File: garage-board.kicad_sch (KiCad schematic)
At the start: 17 parts, among them J1 Input, M1 Motor_DC, U1 Pololu_H2_36v11_CS, U2 ESP32-C6-DEV-KIT-N8, U3 Pololu-5266

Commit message: kicad: claude clean up
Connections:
- net GND: now also HS1.3 (GND), U2.32 (GND), U3.2 (GND); no longer HS1. (GND), U3. (EN)
- net +31V: now reaches C2.1, D1.4 (+), D2.1 (A1), R3.2, U1.9 (VIN)
- net +31V: now also U3.3 (VIN); no longer U3. (EN)
- net at R1.2, R2.1: now also HS1.1 (A); no longer HS1. (GND)
- net PWMB: now reaches U1.2 (PWMB), U2.26 (IO21)
- net PWMA: now reaches U1.3 (PWMA), U2.25 (IO20)
- net ~{SLP}: now reaches U1.4 (~{SLP}), U2.24 (IO19)
- net ~{FLT}: now reaches U1.5 (~{FLT}), U2.23 (IO18)
- net CS: now reaches U1.6 (CS), U2.12 (IO2)
- net 3V3 renamed +3V3
- net +3V3: now also HS1.2 (+), U3.1 (VOUT); no longer HS1. (GND), U3. (EN)
- no-connect marks 0 -> 22
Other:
- note added: "24 V AC"
- note added: "24 V AC INPUT & RECTIFIER"
- note added: "3.3 V REGULATOR"
- note added: "ESP32-C6 MCU"
- note added: "HALL SENSOR"
- note added: "MOTOR DRIVER"
- title: (none) -> Garage board
- moved on the sheet: C1, C2, C3, C4, D1, D2, F1, J1, M1, R1, R2, R3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

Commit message: Change to 5V and power issues
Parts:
- removed M1: Motor_DC, symbol Motor:Motor_DC
- added C5: 470uF 105C ESR, symbol Device:C_Polarized
- added C6: 100nF, symbol Device:C
- added D3: 1N4007, Diode_THT:D_DO-41_SOD81_P10.16mm_Horizontal, symbol Diode:1N4007
- added J2: Motor, symbol Connector_Generic:Conn_01x03
- added J5: btn0, symbol Connector_Generic:Conn_01x02
- added R5: 4.7k, symbol Device:R
- added R6: 1k, symbol Device:R
- C1: value 470uF -> 470uF 105C ESR
- C2: value 470uF -> 4700uF 105C ESR
- C3: value 2.2nF -> 100nF
- HS1: value (none) -> HAL503
- J1: value Input -> 24VAC
- R2: value 1k -> 10k
- R3: value 10k -> 10k (0.5W)
- R4: value 10k -> 4.7k
- U3: value Pololu-5266 -> Pololu-5267; symbol garage_board_symbols:Pololu-5266 -> garage_board_symbols:Pololu-5267
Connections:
- net +31V: now also D3.2 (A); no longer U3.3 (VIN)
- net +3V3: now also R5.1; no longer C4.2, HS1.2 (+), U3.1 (VOUT)
- net GND: now also C5.2, C6.2, J2.3 (Pin_3), J5.1 (Pin_1); no longer C1.2
- net at U1.10 (OUTA): now also J2.2 (Pin_2)
- net at U1.11 (OUTB): now also J2.1 (Pin_1)
- net +5V: now reaches U2.14 (5V)
- net +5V: now also C4.2, HS1.2 (+), U3.1 (VOUT)
- net at U2.5 (IO6): now also C6.1, R5.2, R6.2
- net CS: no longer names the net of U1.6 (CS), U2.12 (IO2)
- net PWMA: no longer names the net of U1.3 (PWMA), U2.25 (IO20)
- net PWMB: no longer names the net of U1.2 (PWMB), U2.26 (IO21)
- net ~{FLT}: no longer names the net of U1.5 (~{FLT}), U2.23 (IO18)
- net ~{SLP}: no longer names the net of U1.4 (~{SLP}), U2.24 (IO19)
- net ~{SLP}: now also R4.1
- new net: J5.2 (Pin_2), R6.1
- new net: C5.1, D3.1 (K), U3.3 (VIN)
- new net: C1.2, U1.13 (-)
- new net: C1.1, U1.14 (+)
- now unconnected: U1.8 (VM)
- no-connect marks 22 -> 21
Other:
- note added: "LOGIC SUPPLY 5 V"
- note removed: "24 V AC"
- note removed: "3.3 V REGULATOR"
- moved on the sheet: C1, D2, R3, U3

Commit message: Add LAMP
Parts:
- added D4: 1N4148, Diode_THT:D_DO-35_SOD27_P7.62mm_Horizontal, symbol Diode:1N4148
- added K1: G5Q-1A, Relay_THT:Relay_SPST_Omron-G5Q-1A, symbol Relay:G5Q-1A
- added LA1: Lamp, symbol Device:Lamp
- added Q1: BC547, Package_TO_SOT_THT:TO-92_Inline, symbol Transistor_BJT:BC547
- added R7: 4.7k, symbol Device:R
- added R8: 680, symbol Device:R
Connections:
- net GND: now also Q1.3 (E)
- net at J1.1 (Pin_1): now also F1.2; no longer D1.3
- net at J1.2 (Pin_2): now also D1.2, K1.3; no longer F1.1
- net at C3.1, R2.2: now also U2.11 (IO11); no longer U2.10 (IO10)
- net at C6.1, R5.2, R6.2: now also U2.10 (IO10); no longer U2.5 (IO6)
- net at C5.1, D3.1 (K), U3.3 (VIN): now also R8.2
- net at U2.6 (IO7): now also R7.2
- net +31V: no longer names the net of C2.1, D1.4 (+), D2.1 (A1), D3.2 (A), R3.2, U1.9 (VIN)
- new net: D4.2 (A), K1.5, Q1.1 (C)
- new net: Q1.2 (B), R7.1
- new net: D1.3, F1.1, LA1.2 (+)
- new net: D4.1 (K), K1.1, R8.1
- new net: K1.2, LA1.1 (-)
- no-connect marks 21 -> 20
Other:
- note added: "24 V AC"
- note added: "LAMP"
- note added: "UHE (or two 2200uF)"
- moved on the sheet: C1, C3, C4, C5, C6, D2, D3, HS1, J2, J5, R1, R2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

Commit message: Fix LED and sW
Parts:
- removed C6: 100nF, symbol Device:C
- removed J5: btn0, symbol Connector_Generic:Conn_01x02
- removed R6: 1k, symbol Device:R
- added D5: Red, symbol Device:LED
- added SW1, SW2, SW3: SW_Push, symbol Switch:SW_Push
- F1: value T8A -> T6.3A
- R5: value 4.7k -> 1k
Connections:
- net +3V3: no longer R5.1
- net GND: now also D5.1 (K), SW2.2, SW3.2
- net at R5.2: now also D5.2 (A); no longer U2.10 (IO10)
- net at U2.27 (IO22): now also SW2.1
- net at U2.28 (IO23): now also SW3.1
- new net: R5.1, U2.10 (IO10)
- no-connect marks 20 -> 18
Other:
- moved on the sheet: C5, D4, F1, K1, LA1, Q1, R4, R7, R8

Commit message: fix layout
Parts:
- removed SW1: SW_Push, symbol Switch:SW_Push
- C1, C5: value 470uF 105C ESR -> 470uF 63V 105C ESR
- C2: value 4700uF 105C ESR -> 4700uF 63V 105C ESR
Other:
- moved on the sheet: C5, D2, D4, D5, K1, LA1, Q1, R1, R3, R4, R5, R7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

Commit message: Add standard footprints
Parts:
- C1, C5: footprint (none) -> Capacitor_THT:CP_Radial_D12.5mm_P5.00mm
- C2: footprint (none) -> garage_board:CP_Radial_D25.0mm_P12.50mm
- C3, C4: footprint (none) -> Capacitor_THT:C_Disc_D5.0mm_W2.5mm_P5.00mm
- HS1: footprint (none) -> Connector_PinHeader_2.54mm:PinHeader_1x03_P2.54mm_Vertical
- J1: footprint (none) -> Connector_Molex:Molex_KK-396_A-41791-0003_1x03_P3.96mm_Vertical; symbol Connector_Generic:Conn_01x02 -> Connector_Generic:Conn_01x03
- J2: footprint (none) -> Connector_Molex:Molex_KK-396_A-41791-0003_1x03_P3.96mm_Vertical
- R1, R2, R4, R5, R7, R8: footprint (none) -> Resistor_THT:R_Axial_DIN0207_L6.3mm_D2.5mm_P10.16mm_Horizontal
- R3: footprint (none) -> Resistor_THT:R_Axial_DIN0414_L11.9mm_D4.5mm_P15.24mm_Horizontal
- U1: value Pololu_H2_36v11_CS -> Pololu-2993
- U2: footprint (none) -> PCM_Espressif:ESP32-C6-DevKitC-1; symbol garage_board_symbols:ESP32-C6-DEV-KIT-N8 -> PCM_Espressif:ESP32-C6-DevKitC-1
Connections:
- net at D1.2, K1.3: now also J1.3 (Pin_3); no longer J1.2 (Pin_2)
- no-connect marks 18 -> 19
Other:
- moved on the sheet: D5, R4, R5, SW2, SW3, U2

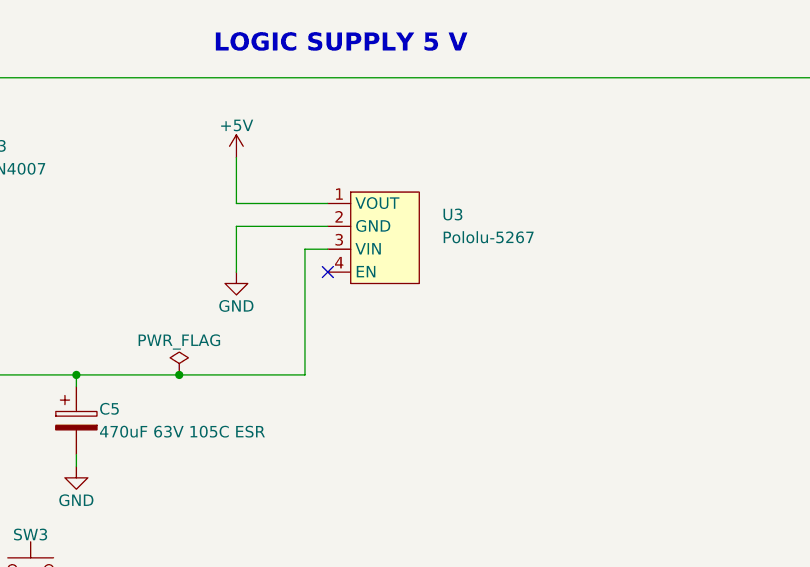
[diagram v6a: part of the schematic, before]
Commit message: Place components sketch on PCB
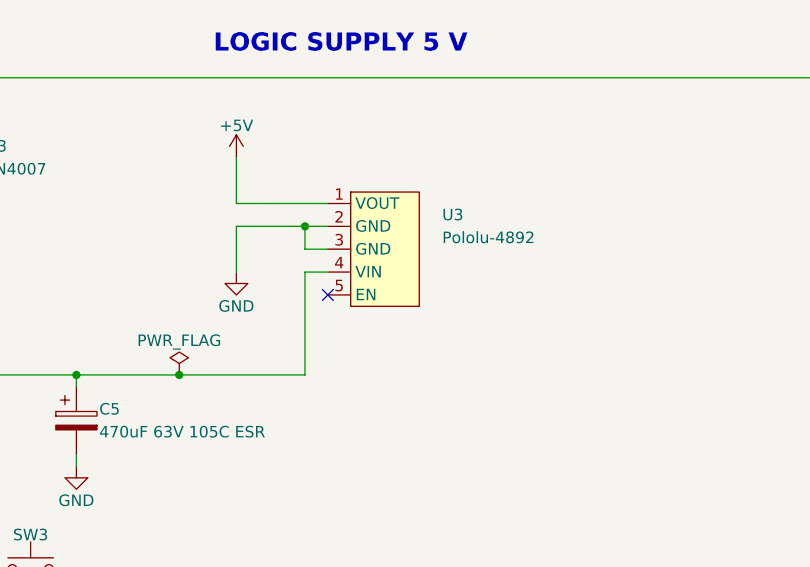
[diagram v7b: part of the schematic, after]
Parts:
- D5: footprint (none) -> garage_board:LED_D5.0mm_Horizontal
- F1: footprint (none) -> garage_board:Fuseholder_5x20mm_Lateral_P20.00x5.00mm
- LA1: footprint (none) -> garage_board:lamp
- SW2, SW3: footprint (none) -> garage_board:Switch
- U1: footprint (none) -> garage_board:Pololu Motor Driver 2993
- U3: value Pololu-5267 -> Pololu-4892; footprint (none) -> garage_board:Pololu 4892
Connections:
- net GND: now also U3.3 (GND)
- net at C5.1, D3.1 (K), R8.2: now also U3.4 (VIN); no longer U3.3 (VIN)
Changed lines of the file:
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@@
 	)
 	(junction
+		(at 210.82 49.53)
+		(diameter 0)
+		(color 0 0 0 0)
+	)
+	(junction
 		(at 27.94 45.72)
 		(diameter 0)
@@
 	)
 	(no_connect
-		(at 213.36 54.61)
+		(at 213.36 57.15)
 	)
 	(no_connect
@@
 	(wire
 		(pts
+			(xy 210.82 66.04) (xy 210.82 54.61)
+		)
+		(stroke
+			(width 0)
+			(type default)
+		)
+	)
+	(wire
+		(pts
 			(xy 165.1 120.65) (xy 170.18 120.65)
 		)
@@
 	(wire
 		(pts
+			(xy 210.82 49.53) (xy 203.2 49.53)
+		)
+		(stroke
+			(width 0)
+			(type default)
+		)
+	)
+	(wire
+		(pts
 			(xy 165.1 92.71) (xy 171.45 92.71)
 		)
@@
 	(wire
 		(pts
-			(xy 213.36 49.53) (xy 203.2 49.53)
+			(xy 213.36 49.53) (xy 210.82 49.53)
 		)
 		(stroke
@@
 	(wire
 		(pts
+			(xy 210.82 49.53) (xy 210.82 52.07)
+		)
+		(stroke
+			(width 0)
+			(type default)
+		)
+	)
+	(wire
+		(pts
 			(xy 185.42 135.89) (xy 185.42 119.38)
 		)
@@
 	(wire
 		(pts
+			(xy 210.82 54.61) (xy 213.36 54.61)
+		)
+		(stroke
+			(width 0)
+			(type default)
+		)
+	)
+	(wire
+		(pts
 			(xy 114.3 125.73) (xy 109.22 125.73)
 		)
@@
 	(wire
 		(pts
-			(xy 210.82 66.04) (xy 210.82 52.07)
-		)
-		(stroke
-			(width 0)
-			(type default)
-		)
-	)
-	(wire
-		(pts
 			(xy 74.93 118.11) (xy 83.82 118.11)
 		)
@@
 			)
 		)
-		(property "Footprint" ""
+		(property "Footprint" "garage_board:Fuseholder_5x20mm_Lateral_P20.00x5.00mm"
 			(at 38.1 63.5 0)
 			(hide yes)
@@
 			)
 		)
-		(property "Footprint" ""
+		(property "Footprint" "garage_board:Switch"
 			(at 189.23 95.25 0)
 			(hide yes)
@@
 			)
 		)
-		(property "Footprint" ""
+		(property "Footprint" "garage_board:Pololu Motor Driver 2993"
 			(at 220.98 116.84 0)
 			(hide yes)
@@
 			)
 		)
-		(property "Footprint" ""
+		(property "Footprint" "garage_board:LED_D5.0mm_Horizontal"
 			(at 85.09 105.41 0)
 			(hide yes)
@@
 			)
 		)
-		(property "Value" "Pololu-5267"
+		(property "Value" "Pololu-4892"
 			(at 226.06 50.8 0)
 			(show_name no)
@@
 			)
 		)
-		(property "Footprint" ""
+		(property "Footprint" "garage_board:Pololu 4892"
 			(at 219.71 50.8 0)
 			(hide yes)
@@
 		(pin "2"
 		)
+		(pin "5"
+		)
 		(instances
 			(project "garage-board"
@@
 			)
 		)
-		(property "Footprint" ""
+		(property "Footprint" "garage_board:lamp"
 			(at 49.53 72.39 0)
 			(hide yes)
@@
 			)
 		)
-		(property "Footprint" ""
+		(property "Footprint" "garage_board:Switch"
 			(at 180.34 87.63 0)
 			(hide yes)
